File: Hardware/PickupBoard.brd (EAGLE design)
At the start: 49.9 x 29 mm, 29 parts, among them U1 TL074_

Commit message: First rev5 upload
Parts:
- removed D1: 1N4148, MusicThingModular:DO35-7
- removed R14: 2.2k, MusicThingModular:7MM_RESISTOR
- removed R16: 220R, MusicThingModular:7MM_RESISTOR
- removed U1: TL074_, MusicThingModular:DIL14
- added C7: 330pf, we-rcl:C0603
- added D3: 1N914.3, gm-diodes:DO35-3
- added R13: 200R, MusicThingModular:7MM_RESISTOR
- added R7: 10K, MusicThingModular:7MM_RESISTOR
- added R9: 32k, MusicThingModular:7MM_RESISTOR
- added U2: TL074_, MusicThingModular:DIL14
- C3: value 470n -> 47n; device TomW:C050-024X044 -> we-rcl:C0603
- C6: value 470pf -> 330pf; device TomW:C050-024X044 -> we-rcl:C0603
- D2: value 1N4148 -> 1N914.3; device MusicThingModular:DO35-7 -> gm-diodes:DO35-3
- JP1: value (none) -> INOUT
- JP2: value M02LOCK -> POT
- R1: value 10k -> 1m
- R10: value 56k -> 200R
- R12: value 2.2k -> 10K
- R2: value 220R -> 10k
- R5: value 1m -> 10k
- R6: value 100k -> 10K
- R8: value 10k -> 150k
- moved D2 64.4 mm to (5.08, -33.0), flipped to the top, turned to 0 degrees
- moved R8 61.1 mm to (1.27, -30.5), flipped to the top, turned to 0 degrees
- moved R4 58.1 mm to (16.5, -29.8), flipped to the top, turned to 0 degrees
- moved R12 57.8 mm to (11.4, -29.8), flipped to the top, turned to 0 degrees
- moved R1 55.7 mm to (22.9, -34.9), flipped to the top, turned to 0 degrees
- moved R6 55.4 mm to (6.35, -29.8), flipped to the top, turned to 0 degrees
- moved R5 54.0 mm to (19.1, -29.8), flipped to the top, turned to 0 degrees
- moved C3 53.6 mm to (3.81, -29.8), flipped to the top
- moved R2 53.1 mm to (14.0, -29.8), flipped to the top, turned to 0 degrees
- moved C6 44.1 mm to (19.1, -18.4), flipped to the top, turned to 0 degrees
- moved R10 42.0 mm to (24.1, -17.8), flipped to the top, turned to 0 degrees
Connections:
- removed net FUZZ_IN: C3.2, R10.1, U1.1, U1.12
- removed net N$1: R5.1, U$1.TIP, U1.3
- removed net N$10: JP1.2, R16.2
- removed net N$5: JP2.2, R14.1
- new net GAIN_IN: R1.2, R2.2, U$1.TIP
- new net N$12: C7.2, R8.1, U2.8
- new net N$15: C6.2, R10.2, R12.1, R5.1, U2.1
- new net N$16: JP1.2, R10.1
- new net N$17: R12.2, U2.5
- new net N$18: R6.2, U2.6, U2.7
- new net N$19: JP1.1, R13.1
- net +12V: now also U2.4; no longer U1.4
- net -12V: now also U2.11; no longer U1.11
- net GND: now also D2.A, D3.C, R1.1, R4.1, R9.1, U2.12; no longer R12.1, R5.2, R8.1, U1.10, U1.5
- net N$11: now also C7.1, R8.2, R9.2, U2.9; no longer R2.1, R6.2, U1.8
- net N$13: now also R13.2; no longer JP1.1, R2.2
- net N$2: now also R2.1, U2.3; no longer C6.2, D1.C, D2.A, R4.2, U1.7
- net N$3: now also U2.13, U2.14; no longer R10.2, R8.2, U1.2
- net N$4: now also C3.2, JP2.2, U2.2; no longer D1.A, D2.C, R1.2, U1.6
- net N$6: now also JP2.1, R5.2; no longer R12.2, R14.2, U1.13
- net N$7: now also R4.2; no longer R1.1
- net N$8: now also R7.1, U2.10; no longer JP2.1, R16.1, U1.14
- net N$9: now also D2.C, D3.A, R7.2; no longer R4.1, U1.9
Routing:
- net N$1: track 43.3 -> 0.00 mm
- net N$6: track 36.7 -> 0.00 mm, vias 1 -> 0
- net FUZZ_IN: track 32.1 -> 0.00 mm
- net N$11: track 26.2 -> 0.00 mm
- net N$2: track 21.0 -> 0.00 mm
- net N$9: track 19.7 -> 0.00 mm
- net N$5: track 19.2 -> 0.00 mm
- net N$8: track 18.5 -> 0.00 mm
- net N$4: track 17.0 -> 0.00 mm
- net N$3: track 14.5 -> 0.00 mm
- net N$13: track 11.0 -> 0.00 mm
- net N$10: track 7.08 -> 0.00 mm
- net +12V: track 25.2 -> 18.9 mm
- net N$7: track 4.97 -> 0.00 mm
- net -12V: track 20.8 -> 18.1 mm
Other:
- board text added: "Revision 5 PCB"
- board text removed: "Revision 4 PCB"

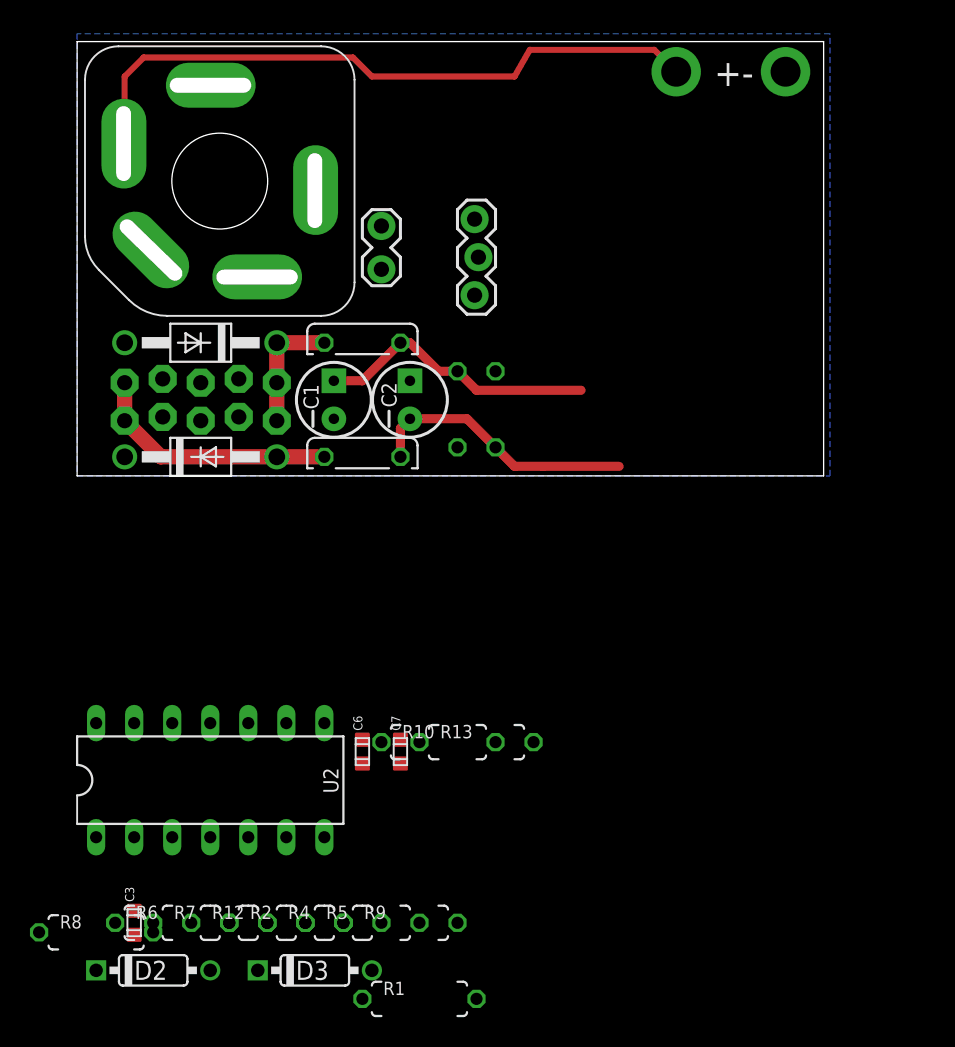
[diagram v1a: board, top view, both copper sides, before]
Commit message: roughly on the board not routed
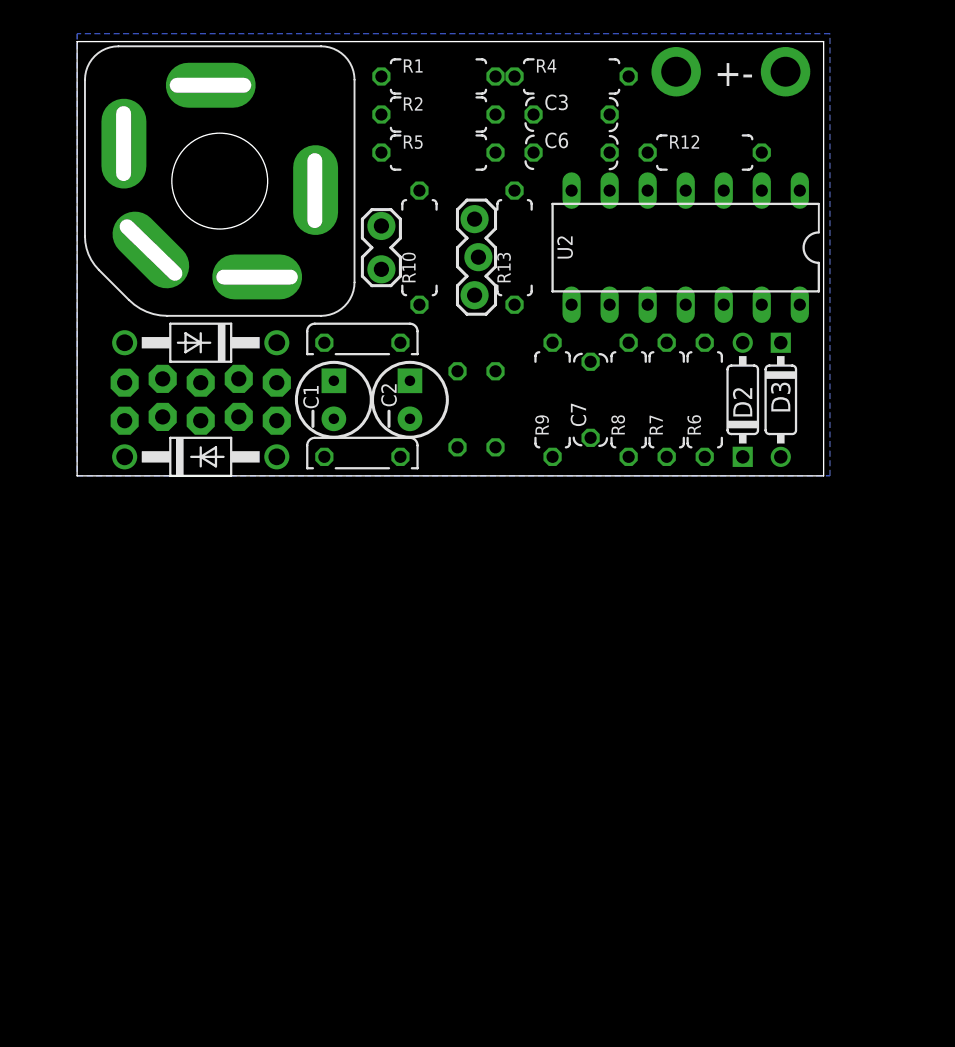
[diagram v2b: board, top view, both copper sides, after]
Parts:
- C3, C6, C7: device we-rcl:C0603 -> TomW:C050-024X044
- moved R1 61.6 mm to (24.1, 26.7)
- moved C3 61.4 mm to (33.0, 24.1)
- moved R12 59.8 mm to (41.9, 21.6)
- moved R4 58.9 mm to (33.0, 26.7)
- moved R2 54.9 mm to (24.1, 24.1)
- moved D2 54.8 mm to (44.5, 5.08), turned to 90 degrees
- moved R5 51.7 mm to (24.1, 21.6)
- moved R8 50.3 mm to (36.8, 5.08), turned to 90 degrees
- moved R6 49.8 mm to (41.9, 5.08), turned to 90 degrees
- moved D3 49.2 mm to (47.0, 5.08), turned to 270 degrees
- moved U2 47.7 mm to (40.6, 15.2), turned to 180 degrees
- moved R7 46.4 mm to (39.4, 5.08), turned to 90 degrees
- moved C6 42.4 mm to (33.0, 21.6)
- moved R9 36.4 mm to (31.8, 5.08), turned to 90 degrees
- moved R13 33.1 mm to (29.2, 15.2), turned to 90 degrees
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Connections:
- net GAIN_IN: now also R1.1, R2.1; no longer R1.2, R2.2
- net GND: now also R1.2; no longer R1.1
- net N$15: now also R12.2; no longer R12.1
- net N$17: now also R12.1; no longer R12.2
- net N$2: now also R2.2; no longer R2.1
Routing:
- net N$14: track 44.0 -> 0.00 mm
- net +12V: track 18.9 -> 0.00 mm
- net -12V: track 18.1 -> 0.00 mm
- net -12V_INLET: track 16.9 -> 0.00 mm
- net +12V_INLET: track 8.38 -> 0.00 mm

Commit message: Designed and routed
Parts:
- removed C3: 47n, TomW:C050-024X044
- removed JP2: POT, SparkFun-Connectors:1X02_LOCK
- removed R4: 10k, MusicThingModular:7MM_RESISTOR
- added CLN, GRND: M01PTH, SparkFun-Connectors:1X01
- C6, C7: device TomW:C050-024X044 -> gm-caps-ceramic:050X030_025
- JP1: value INOUT -> (none); device SparkFun-Connectors:1X03_LOCK -> SparkFun-Connectors:1X03
- moved C5 30.5 mm to (50.2, 25.4), turned to 45 degrees
- moved R2 22.2 mm to (46.4, 24.8), flipped to the bottom, turned to 45 degrees
- moved JP4 22.2 mm to (25.1, 27.0)
- moved C7 19.7 mm to (54.0, 3.81), flipped to the bottom, turned to 135 degrees
- moved C1 19.7 mm to (27.9, 21.6), turned to 180 degrees
- moved JP3 19.1 mm to (21.0, 27.0)
- moved R1 18.5 mm to (42.5, 24.8), flipped to the bottom, turned to 45 degrees
- moved C4 17.8 mm to (43.2, 5.71), turned to 135 degrees
- moved R9 17.2 mm to (48.9, 5.71), flipped to the bottom, turned to 135 degrees
- moved C2 16.5 mm to (22.2, 21.6), turned to 180 degrees
- moved R8 15.3 mm to (52.1, 5.71), flipped to the bottom, turned to 135 degrees
- moved FUSE 13.4 mm to (20.3, 14.6), turned to 90 degrees
- moved D3 13.4 mm to (33.7, 5.71), flipped to the bottom, turned to 315 degrees
- moved U$2 13.3 mm to (21.6, 5.08)
- moved R5 11.5 mm to (35.2, 24.4), flipped to the bottom, turned to 45 degrees
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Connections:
- removed net N$13: R13.2
- removed net N$16: JP1.2, R10.1
- removed net N$19: JP1.1, R13.1
- removed net N$4: C3.2, C6.1, JP2.2, U2.2
- removed net N$6: JP2.1, R5.2
- removed net N$7: C3.1, R4.2
- new net CLEAN: CLN.1, R10.2
- new net END: C6.1, JP1.2, U2.9
- new net FUZZ: JP1.3, R13.2
- new net WIPER: JP1.1, R5.1
- net -12V: now also C5.1; no longer C5.2
- net GAIN_IN: now also R1.2, R2.2; no longer R1.1, R2.1
- net GND: now also C5.2, GRND.1, R1.1; no longer C5.1, JP1.3, R1.2, R4.1
- net N$11: now also R8.1, U2.2; no longer R8.2, U2.9
- net N$12: now also R13.1, R8.2, U2.1; no longer R8.1, U2.8
- net N$15: now also R10.1, R5.2, U2.8; no longer R10.2, R5.1, U2.1
- net N$2: now also R2.1, U2.10; no longer R2.2, U2.3
- net N$8: now also R7.2, U2.3; no longer R7.1, U2.10
- net N$9: now also R7.1; no longer R7.2
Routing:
- net +12V: track 0.00 -> 42.5 mm
- net -12V: track 0.00 -> 40.2 mm
- net GAIN_IN: track 0.00 -> 37.3 mm
- net N$12: track 0.00 -> 32.9 mm
- net CLEAN: track 0.00 -> 25.2 mm
- net +12V_INLET: track 0.00 -> 24.6 mm
- net N$15: track 0.00 -> 23.9 mm
- net END: track 0.00 -> 22.4 mm
- net N$14: track 0.00 -> 19.8 mm
- net WIPER: track 0.00 -> 18.4 mm
- net -12V_INLET: track 0.00 -> 16.3 mm
- net N$17: track 0.00 -> 13.1 mm
- net N$9: track 0.00 -> 13.0 mm
- net N$11: track 0.00 -> 12.4 mm
- net FUZZ: track 0.00 -> 9.55 mm
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- added copper zone on layer 1, net GND
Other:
- board size 49.9 x 29 mm -> 56.2 x 29 mm

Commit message: Rev5  with gerbers
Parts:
- turned R10 to 90 degrees
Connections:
- net CLEAN: now also R10.1; no longer R10.2
- net N$15: now also R10.2; no longer R10.1
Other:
- board text added: "+ -"
- board text added: "Music Thing Modular Electrophone Main PCB CC-BY-SA Tom Whitwell, Herne Hill, London"
- board text added: "Revision 5 PCB August 2017"
- board text removed: "+-"
- board text removed: "Music Thing Modular Electrophone Back PCB CC-BY-SA Tom Whitwell Herne Hill, London"
- board text removed: "Revision 5 PCB"
